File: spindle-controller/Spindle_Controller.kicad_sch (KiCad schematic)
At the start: 24 parts, among them J1 Conn_01x19, J10 Conn_01x03, J11 Conn_01x02, J12 Conn_01x04, J13 Conn_01x02, J14 Conn_01x04, J15 GX12-6, J17 LEMO2, J18 LEMO2, J19 GX12-4, J2 Conn_01x19, J26 GX12-2, J3 Conn_01x14, J4 Jack-DC, J5 USB_C_Receptacle_USB2.0_16P, J6 Conn_01x04, J7 Conn_01x04, J8 Conn_01x04, J9 Conn_01x05, K2 JQC-3FF-005-1Z, K3 JQC-3FF-005-1Z, K4 JQC-3FF-005-1Z, K5 JQC-3FF-005-1Z, SW1 DPDT Toggle Switch

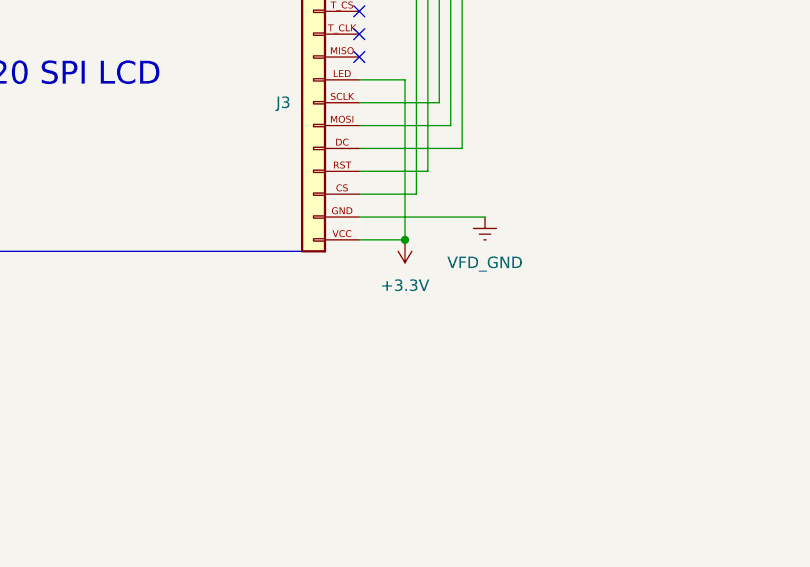
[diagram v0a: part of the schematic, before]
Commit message: changed 5.5 to 5v on display
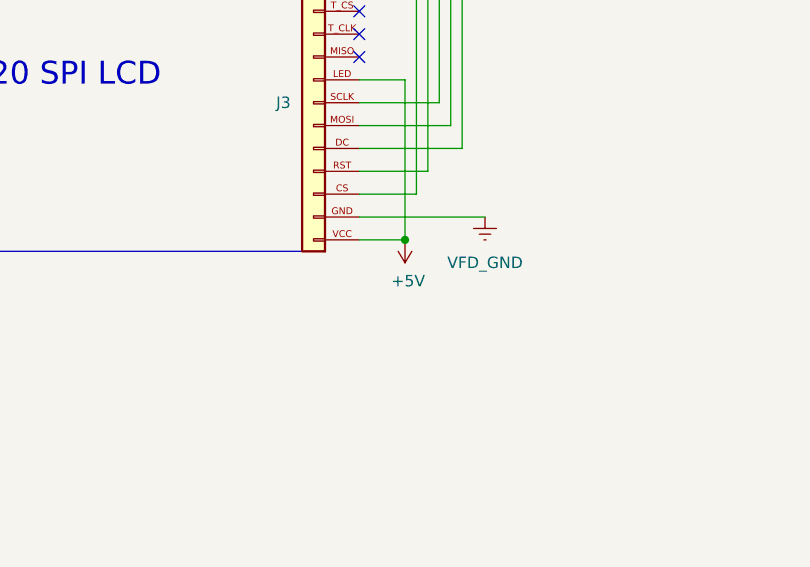
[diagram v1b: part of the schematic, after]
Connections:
- net +3.3V: no longer J3.LED (Pin_8), J3.VCC (Pin_1)
- net +5V: now also J3.LED (Pin_8), J3.VCC (Pin_1)
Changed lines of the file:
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@@
 		(in_pos_files yes)
 		(dnp no)
-		(fields_autoplaced yes)
 		(property "Reference" "#PWR011"
 			(at 251.46 146.05 0)
@@
 			)
 		)
-		(property "Value" "+3.3V"
-			(at 251.46 154.94 0)
+		(property "Value" "+5V"
+			(at 249.936 154.432 0)
 			(show_name no)
 			(do_not_autoplace no)
@@
 					(size 1.27 1.27)
 				)
+				(justify right)
 			)
 		)

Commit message: updated connectors
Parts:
- removed J17, J18: LEMO2, symbol Connector:LEMO2
- added J20, J21: DIN-3, symbol Connector:DIN-3
- J15: value GX12-6 -> GX12-7
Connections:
- net LED_GREEN: now also J19.4
- net LED_RED: no longer J19.4
- net VFD_GND: now also J20.3, J21.3
- net at K5.14: now also J21.1
- net at K4.14: now also J20.1
- no-connect marks 13 -> 23
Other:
- note added: "Din-3"
- note added: "Programming Data"
- note removed: "Progrsmming Data"

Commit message: more cleanup
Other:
- note added: "VFD_DI1 gets it's input from TechnoCNC conroller relay (SPINDLE_CMD) It is the "turn on motor" signal"
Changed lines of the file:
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@@
+		)
+	)
+	(text "VFD_DI1 gets it's input from TechnoCNC \nconroller relay (SPINDLE_CMD)\nIt is the \"turn on motor\" signal"
+		(exclude_from_sim no)
+		(at 136.652 255.778 0)
+		(effects
+			(font
+				(size 1.27 1.27)
+			)
+			(justify left)
 		)
 	)
@@
 	)
 	(junction
+		(at 182.88 218.44)
+		(diameter 0)
+		(color 0 0 0 0)
+	)
+	(junction
 		(at 194.056 66.802)
 		(diameter 0)
@@
 		(color 0 0 0 0)
 	)
+	(junction
+		(at 182.88 233.172)
+		(diameter 0)
+		(color 0 0 0 0)
+	)
 	(no_connect
 		(at 128.27 77.47)
@@
 	(wire
 		(pts
+			(xy 158.75 218.44) (xy 182.88 218.44)
+		)
+		(stroke
+			(width 0)
+			(type default)
+		)
+	)
+	(wire
+		(pts
 			(xy 213.0911 23.591) (xy 254 23.591)
 		)
@@
 	(wire
 		(pts
+			(xy 182.88 233.172) (xy 182.88 235.204)
+		)
+		(stroke
+			(width 0)
+			(type default)
+		)
+	)
+	(wire
+		(pts
 			(xy 72.39 40.64) (xy 72.39 54.61)
 		)
@@
 	(wire
 		(pts
-			(xy 182.88 233.172) (xy 182.88 235.204)
-		)
-		(stroke
-			(width 0)
-			(type default)
-		)
-	)
-	(wire
-		(pts
 			(xy 21.59 80.01) (xy 35.56 80.01)
 		)
@@
 	(wire
 		(pts
+			(xy 182.88 218.44) (xy 182.88 233.172)
+		)
+		(stroke
+			(width 0)
+			(type default)
+		)
+	)
+	(wire
+		(pts
 			(xy 234.169 49.022) (xy 234.169 50.7878)
 		)
@@
 		(pts
 			(xy 208.026 36.2764) (xy 208.026 18.4964)
+		)
+		(stroke
+			(width 0)
+			(type default)
+		)
+	)
+	(wire
+		(pts
+			(xy 182.88 217.17) (xy 182.88 218.44)
 		)
 		(stroke
@@
 	(global_label "VFD_COM"
 		(shape input)
-		(at 182.88 233.172 90)
+		(at 182.88 217.17 0)
 		(fields_autoplaced yes)
 		(effects
@@
 		)
 		(property "Intersheetrefs" "${INTERSHEET_REFS}"
-			(at 182.88 221.2441 90)
+			(at 194.8079 217.17 0)
 			(hide yes)
 			(show_name no)
@@
 			)
 		)
-	)
-	(global_label "VFD_COM"
-		(shape input)
-		(at 158.75 218.44 0)
-		(fields_autoplaced yes)
-		(effects
-			(font
-				(size 1.27 1.27)
-				(thickness 0.254)
-				(bold yes)
-			)
-			(justify left)
-		)
-		(property "Intersheetrefs" "${INTERSHEET_REFS}"
-			(at 170.6779 218.44 0)
-			(hide yes)
-			(show_name no)
-			(do_not_autoplace no)
-			(effects
-				(font
-					(size 1.27 1.27)
-				)
-				(justify left)
-			)
-		)

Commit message: wire colors
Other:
- note added: "BLUE WIRE"
- note added: "Blue Wire"
- note added: "Brown Wire"
- note added: "Green Wire"
- note added: "Grey Wire"
- note added: "Orange Wire"
- note added: "Red Wire"
- note added: "White Wire"
- note added: "Yellow Wire"

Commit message: updated cable colors
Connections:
- no-connect marks 23 -> 22
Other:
- note added: "(Cable black)"
- note added: "(Cable red)"
- note added: "Cable Black"
- note added: "Cable Red"
- note added: "Cable White"
- note added: "Cable Yellow"
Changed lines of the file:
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@@
+		)
+	)
+	(text "(Cable red)"
+		(exclude_from_sim no)
+		(at 137.668 172.72 90)
+		(effects
+			(font
+				(size 1.27 1.27)
+			)
 		)
 	)
@@
 		)
 	)
+	(text "(Cable black)"
+		(exclude_from_sim no)
+		(at 127.254 173.228 90)
+		(effects
+			(font
+				(size 1.27 1.27)
+			)
+		)
+	)
 	(text "Brown Wire"
 		(exclude_from_sim no)
@@
 		)
 	)
+	(text "Cable Yellow"
+		(exclude_from_sim no)
+		(at 46.482 245.872 90)
+		(effects
+			(font
+				(size 1.27 1.27)
+			)
+		)
+	)
 	(text "Green Wire"
 		(exclude_from_sim no)
@@
 				(size 1.27 1.27)
 				(italic yes)
+			)
+		)
+	)
+	(text "Cable White"
+		(exclude_from_sim no)
+		(at 55.118 245.618 90)
+		(effects
+			(font
+				(size 1.27 1.27)
 			)
 		)
@@
 		)
 	)
+	(text "Cable Black"
+		(exclude_from_sim no)
+		(at 61.722 223.266 90)
+		(effects
+			(font
+				(size 1.27 1.27)
+			)
+		)
+	)
 	(text "Green Wire"
 		(exclude_from_sim no)
@@
 		)
 	)
+	(text "(Cable red)"
+		(exclude_from_sim no)
+		(at 108.204 172.72 90)
+		(effects
+			(font
+				(size 1.27 1.27)
+			)
+		)
+	)
 	(text "Blue Wire"
 		(exclude_from_sim no)
@@
 		)
 	)
+	(text "(Cable black)"
+		(exclude_from_sim no)
+		(at 156.972 173.228 90)
+		(effects
+			(font
+				(size 1.27 1.27)
+			)
+		)
+	)
 	(text "Red Wire"
 		(exclude_from_sim no)
@@
 		)
 	)
+	(text "Cable Red"
+		(exclude_from_sim no)
+		(at 46.228 224.028 90)
+		(effects
+			(font
+				(size 1.27 1.27)
+			)
+		)
+	)
 	(text "Relay #2"
 		(exclude_from_sim no)
@@
 	)
 	(no_connect
-		(at 177.8 187.96)
-	)
-	(no_connect
